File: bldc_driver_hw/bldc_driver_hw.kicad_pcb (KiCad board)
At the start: 2 copper layers, 100 x 150 mm, 285 parts, among them J1 Conn_01x02, J2 USB_C_Receptacle_USB2.0_16P, J3 JTAG_CONN, J4 USB_C_Receptacle_USB2.0_16P, J5 Conn_01x03_Pin, J6 Conn_01x03_Pin, J7 Conn_01x03, J9 Conn_01x02, Q1 IPB026N06NATMA1, Q2 IPB026N06NATMA1, Q3 IPB026N06NATMA1, Q4 IPB026N06NATMA1, Q5 IPB026N06NATMA1, Q6 IPB026N06NATMA1, SW1 SW_Push, SW2 SW_Push, SW3 SW_Push, U10 INA240A1D, U11 INA240A1D, U12 SN65HVD234, U13 MCP6569, U14 TPS54360DDA, U15 UCC27288, U16 UCC27288, U17 UCC27288, U2 USBLC6-2SC6, U3 TPS562201DDCR, U4 AMS1117-3.3, U5 MCP1501-33xSN, U6 STM32G474RETx, U7 USBLC6-2SC6, U8 ESP32-C6-MINI-1, U9 INA240A1D, Y1 24MHz

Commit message: Changed size of capacitors at input 48V dc converter
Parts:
- C3, C4: footprint Capacitor_SMD:C_0805_2012Metric -> Capacitor_SMD:C_1210_3225Metric
- C5: value 100nF -> 100nF 75V; footprint Capacitor_SMD:C_0603_1608Metric -> Capacitor_SMD:C_0805_2012Metric
- R4, R5, R6, R7: footprint Capacitor_SMD:C_0603_1608Metric -> Resistor_SMD:R_0603_1608Metric
- moved C4 5.13 mm to (110.0, 148.8), turned to 180 degrees
- moved C3 0.88 mm to (111.6, 143.2)
- moved C12 0.20 mm to (116.0, 142.4)
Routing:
- net GND: vias 780 -> 782

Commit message: changed vref
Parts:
- removed U5: MCP1501-33xSN, Package_SO:SOIC-8_3.9x4.9mm_P1.27mm
- added C101: 1uF, Capacitor_SMD:C_0603_1608Metric, F.Cu at (126.6, 88.0)
- added J10: MR60_F, Connector_Phoenix_GMSTB:PhoenixContact_GMSTBVA_2,5_3-G_1x03_P7.50mm_Vertical, F.Cu at (201.6, 89.3)
- added U1: TS3333ACR, Package_TO_SOT_SMD:SOT-23-3, F.Cu at (124.1, 86.1)
- moved C40 27.8 mm to (198.0, 145.0), turned to 180 degrees
- moved J9 14.0 mm to (175.0, 157.6)
- moved TP11 2.30 mm to (123.6, 82.1)
- moved C19 1.98 mm to (119.9, 88.0)
- moved C20 1.98 mm to (121.6, 88.0)
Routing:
- net GND: track 167.1 -> 209.6 mm, vias 782 -> 779
- net /BEMF_SENS/PHASE_U: track 89.9 -> 99.3 mm, vias 4 -> 16
- net +5V: track 25.4 -> 20.0 mm
- net Net-(U6-VREF+): track 9.05 -> 11.3 mm
- net VDD: track 46.0 -> 47.3 mm
- net Net-(JP5-A): track 7.87 -> 8.89 mm
- net /BEMF_SENS/PHASE_W: vias 2 -> 16
- net /BEMF_SENS/PHASE_V: vias 2 -> 12
- net +48V: vias 125 -> 124
- added copper zone on B.Cu, net /BEMF_SENS/PHASE_U
- added copper zone on B.Cu, net /BEMF_SENS/PHASE_V
- added copper zone on B.Cu, net /BEMF_SENS/PHASE_W

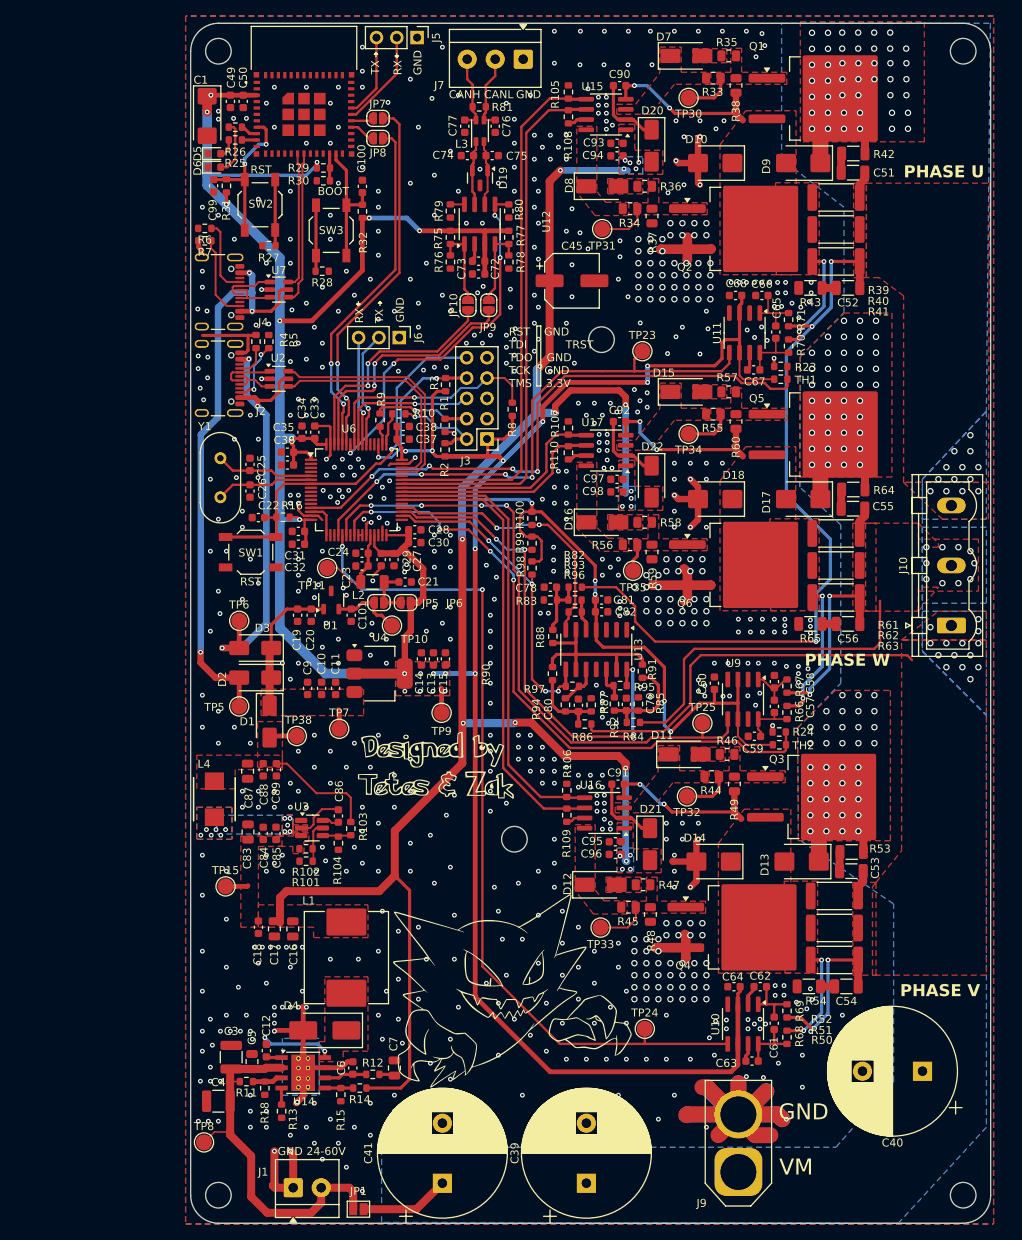
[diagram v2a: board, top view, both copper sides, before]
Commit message: changed hrtim to tim1
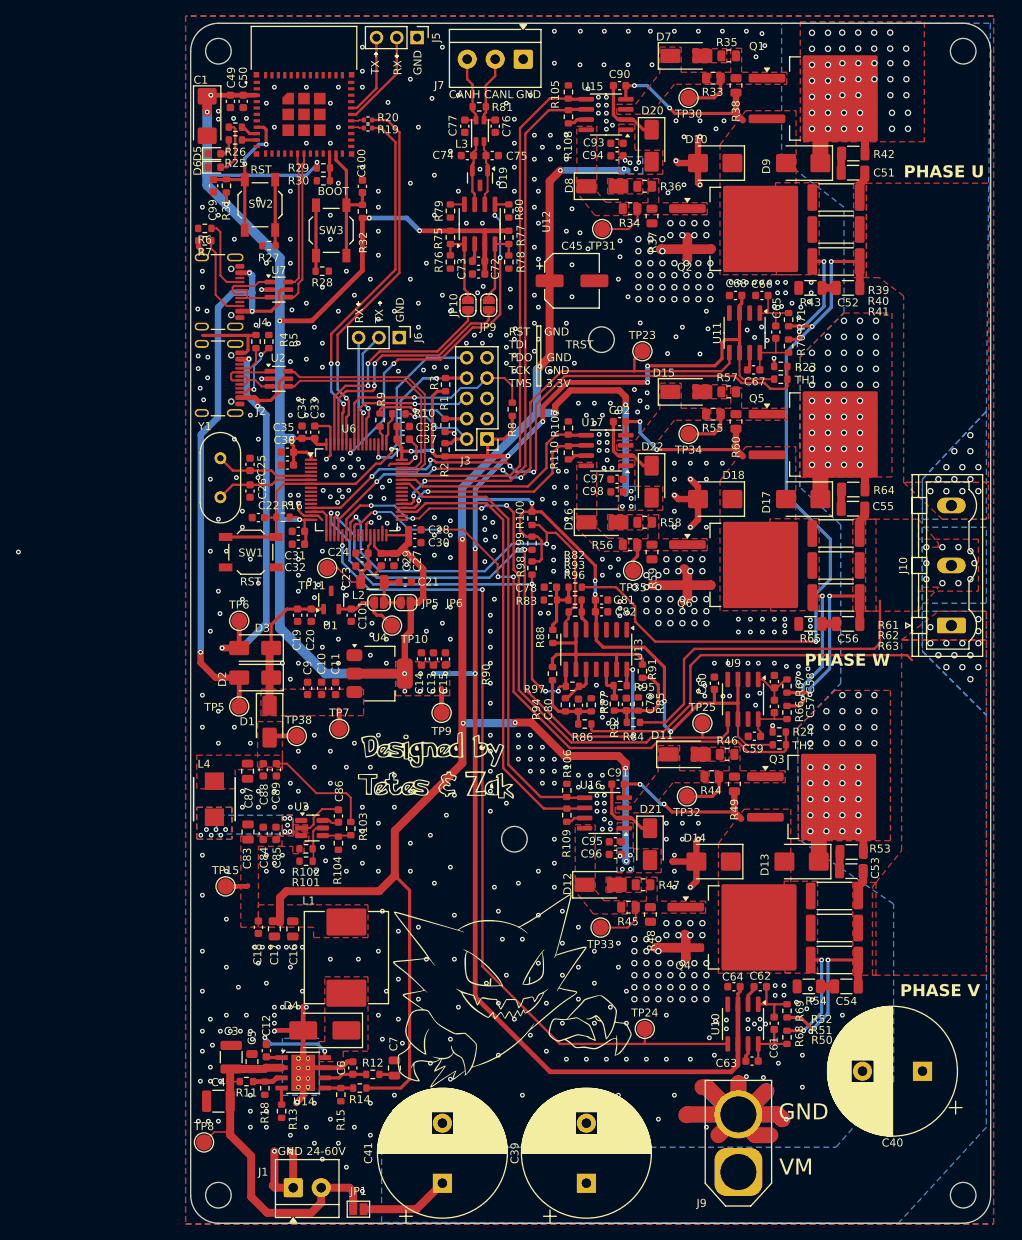
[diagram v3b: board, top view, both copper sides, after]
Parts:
- removed JP7, JP8: SolderJumper_2_Open, Jumper:SolderJumper-2_P1.3mm_Open_RoundedPad1.0x1.5mm
- added R19: 0R, Resistor_SMD:R_0402_1005Metric, F.Cu at (128.7, 27.1)
- added R20: 0R, Resistor_SMD:R_0402_1005Metric, F.Cu at (128.7, 26.1)
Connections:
- U6 pad 18: unconnected-(U6-PA4-Pad18) -> /BEMF_SENS/BEMF_W
- U6 pad 19: unconnected-(U6-PA5-Pad19) -> /BEMF_SENS/BEMF_V
- U6 pad 23: unconnected-(U6-PC5-Pad23) -> /BEMF_SENS/BEMF_U
- U6 pad 34: /BEMF_SENS/BEMF_W -> unconnected-(U6-PB12-Pad34)
- U6 pad 35: /BEMF_SENS/BEMF_V -> /MCU/IN_L_W
- U6 pad 36: /BEMF_SENS/BEMF_U -> /MCU/IN_L_V
- U6 pad 37: /MCU/H_BRIDGE_IRQ -> /MCU/IN_L_U
- U6 pad 38: /MCU/IN_L_W -> unconnected-(U6-PC6-Pad38)
- U6 pad 39: /MCU/IN_H_W -> unconnected-(U6-PC7-Pad39)
- U6 pad 40: /MCU/IN_L_V -> unconnected-(U6-PC8-Pad40)
- U6 pad 41: /MCU/IN_H_V -> unconnected-(U6-PC9-Pad41)
- U6 pad 42: /MCU/IN_L_U -> /MCU/IN_H_W
- U6 pad 43: /MCU/IN_H_U -> /MCU/IN_H_V
- U6 pad 44: unconnected-(U6-PA10-Pad44) -> /MCU/IN_H_U
- U6 pad 59: Net-(JP7-A) -> /MCU/UART_MOTOR_TX
- U6 pad 60: Net-(JP8-A) -> /MCU/UART_MOTOR_RX
- U8 pad 28: /MCU/UART_MOTOR_RX -> Net-(U8-IO22)
- U8 pad 29: /MCU/UART_MOTOR_TX -> Net-(U8-IO23)
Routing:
- net Net-(JP7-A): track 46.2 -> 0.00 mm, vias 2 -> 0
- net /MCU/UART_MOTOR_TX: track 2.82 -> 47.0 mm, vias 0 -> 2
- net Net-(JP8-A): track 43.5 -> 0.00 mm, vias 2 -> 0
- net /MCU/UART_MOTOR_RX: track 3.28 -> 45.5 mm, vias 0 -> 2
- net /BEMF_SENS/BEMF_U: track 35.4 -> 51.3 mm
- net /BEMF_SENS/BEMF_V: track 62.9 -> 78.4 mm
- net /BEMF_SENS/BEMF_W: track 40.3 -> 54.4 mm
- net GND: track 209.6 -> 212.4 mm, vias 779 -> 782
- net Net-(U8-IO22): track 0.00 -> 1.63 mm
- net Net-(U8-IO23): track 0.00 -> 1.63 mm
- net /MCU/IN_L_V: track 26.9 -> 28.2 mm, vias 0 -> 2
- net /MCU/ADC_CSA_V: track 79.2 -> 80.6 mm
- net /MCU/IN_L_U: track 67.6 -> 68.7 mm, vias 0 -> 2
- net /MCU/TEMP_SENS1: track 75.2 -> 76.2 mm
- net /MCU/IN_H_W: track 56.5 -> 57.1 mm
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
